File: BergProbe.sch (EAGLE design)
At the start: 16 parts, among them Q1 DMG6602SVT, Q2 DMG6602SVT, U1 DS3231SN

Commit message: Initial (incomplete) PCB Layout.
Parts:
- renumbered R5 to R500, R6 to R600
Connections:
- removed net BATTERY: R500.1, R600.2, U$1.BAT
- net SAT_BAT: now also R500.1, R600.2, U$1.BAT
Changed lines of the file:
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@@
 <part name="GND10" library="supply1" deviceset="GND" device=""/>
 <part name="Q1" library="farnell-parts" deviceset="DMG6602SVT" device=""/>
-<part name="R5" library="resistor" deviceset="R-EU_" device="R0805" value="DNP"/>
-<part name="R6" library="resistor" deviceset="R-EU_" device="R0805" value="DNP"/>
+<part name="R500" library="resistor" deviceset="R-EU_" device="R0805" value="DNP"/>
+<part name="R600" library="resistor" deviceset="R-EU_" device="R0805" value="DNP"/>
 </parts>
 <sheets>
@@
 <instance part="Q1" gate="G$1" x="342.9" y="190.5"/>
 <instance part="Q1" gate="G$2" x="347.98" y="198.12"/>
-<instance part="R5" gate="G$1" x="119.38" y="50.8" rot="R180"/>
-<instance part="R6" gate="G$1" x="134.62" y="50.8" rot="R180"/>
+<instance part="R500" gate="G$1" x="119.38" y="50.8" rot="R180"/>
+<instance part="R600" gate="G$1" x="134.62" y="50.8" rot="R180"/>
 </instances>
 <busses>
 </busses>
 <nets>
-<net name="BATTERY" class="0">
-<segment>
-<pinref part="U$1" gate="G$1" pin="BAT"/>
-<wire x1="38.1" y1="218.44" x2="38.1" y2="246.38" width="0.1524" layer="91"/>
-<label x="38.1" y="233.68" size="1.778" layer="95" rot="R90"/>
-</segment>
-<segment>
-<pinref part="R6" gate="G$1" pin="2"/>
-<pinref part="R5" gate="G$1" pin="1"/>
-<wire x1="129.54" y1="50.8" x2="127" y2="50.8" width="0.1524" layer="91"/>
-<wire x1="127" y1="50.8" x2="124.46" y2="50.8" width="0.1524" layer="91"/>
-<wire x1="127" y1="50.8" x2="127" y2="35.56" width="0.1524" layer="91"/>
-<label x="127" y="35.56" size="1.778" layer="95" rot="R90"/>
-</segment>
-</net>
 <net name="GND" class="0">
 <segment>
@@
 </segment>
 <segment>
-<pinref part="R5" gate="G$1" pin="2"/>
-<wire x1="114.3" y1="50.8" x2="101.6" y2="50.8" width="0.1524" layer="91"/>
+<pinref part="R500" gate="G$1" pin="2"/>
+<wire x1="114.3" y1="50.8" x2="111.76" y2="50.8" width="0.1524" layer="91"/>
 <label x="101.6" y="50.8" size="1.778" layer="95"/>
+<wire x1="111.76" y1="50.8" x2="101.6" y2="50.8" width="0.1524" layer="91"/>
+<wire x1="111.76" y1="50.8" x2="111.76" y2="48.26" width="0.1524" layer="91"/>
+<pinref part="R600" gate="G$1" pin="2"/>
+<pinref part="R500" gate="G$1" pin="1"/>
+<wire x1="129.54" y1="50.8" x2="127" y2="50.8" width="0.1524" layer="91"/>
+<wire x1="127" y1="50.8" x2="124.46" y2="50.8" width="0.1524" layer="91"/>
+<wire x1="127" y1="50.8" x2="127" y2="48.26" width="0.1524" layer="91"/>
+<label x="127" y="35.56" size="1.778" layer="95" rot="R90"/>
+<wire x1="127" y1="48.26" x2="127" y2="35.56" width="0.1524" layer="91"/>
+<wire x1="111.76" y1="48.26" x2="127" y2="48.26" width="0.1524" layer="91"/>
+<junction x="111.76" y="50.8"/>
+<junction x="127" y="48.26"/>
+</segment>
+<segment>
+<pinref part="U$1" gate="G$1" pin="BAT"/>
+<wire x1="38.1" y1="218.44" x2="38.1" y2="246.38" width="0.1524" layer="91"/>
+<label x="38.1" y="233.68" size="1.778" layer="95" rot="R90"/>
 </segment>
 </net>
@@
 </segment>
 <segment>
-<pinref part="R6" gate="G$1" pin="1"/>
+<pinref part="R600" gate="G$1" pin="1"/>
 <wire x1="139.7" y1="50.8" x2="152.4" y2="50.8" width="0.1524" layer="91"/>
 <label x="142.24" y="50.8" size="1.778" layer="95"/>

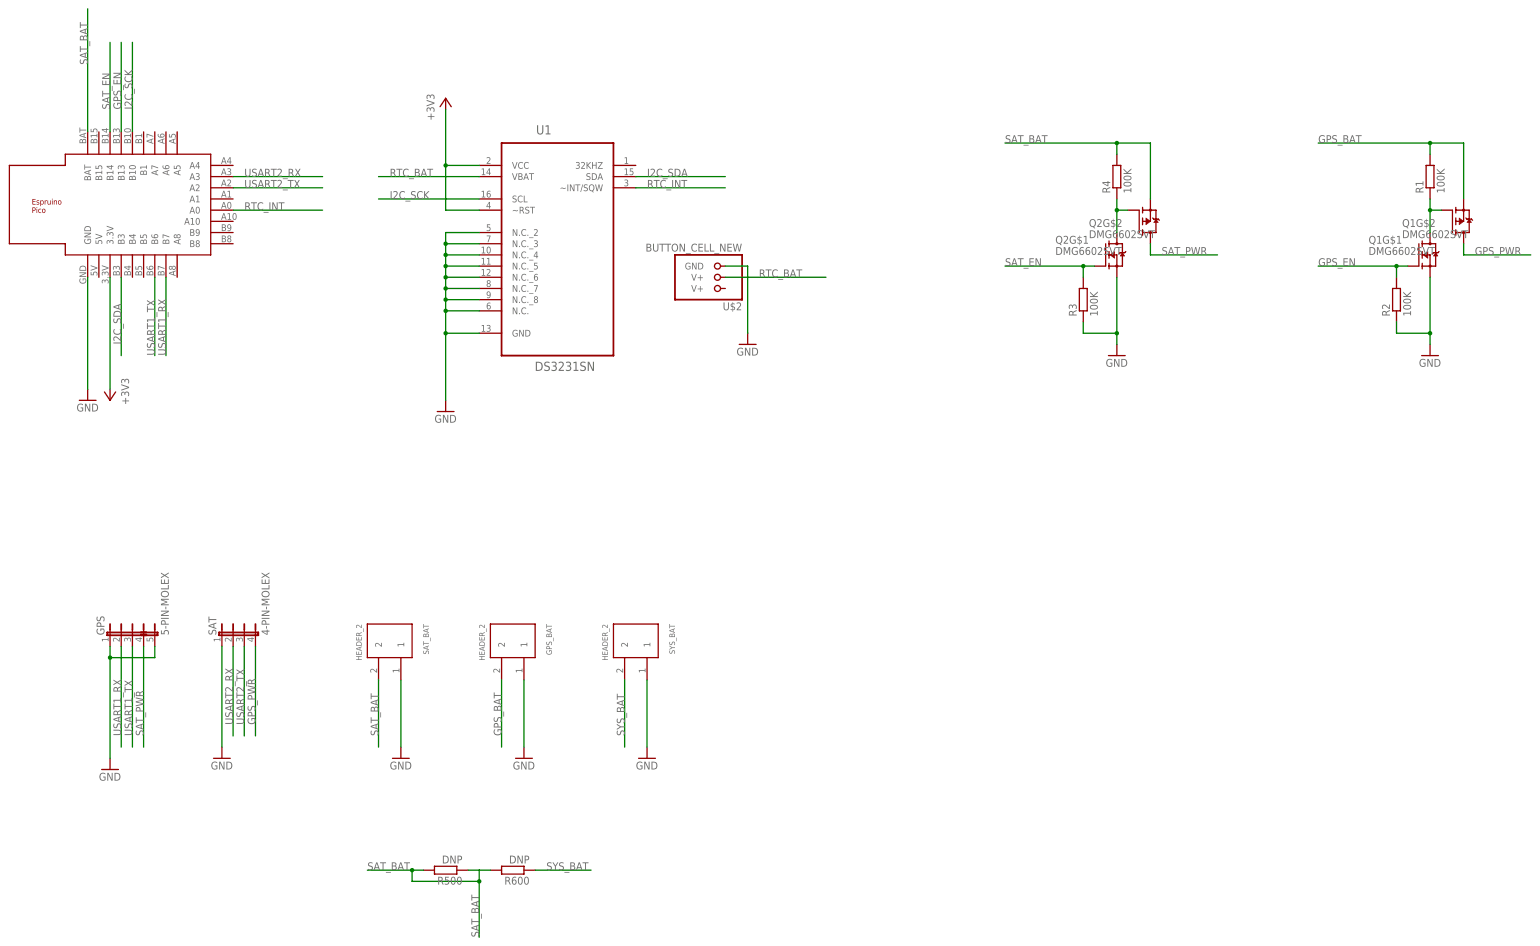
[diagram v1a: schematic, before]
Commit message: Progress on PCB layout. Added analogue headers to schematic.
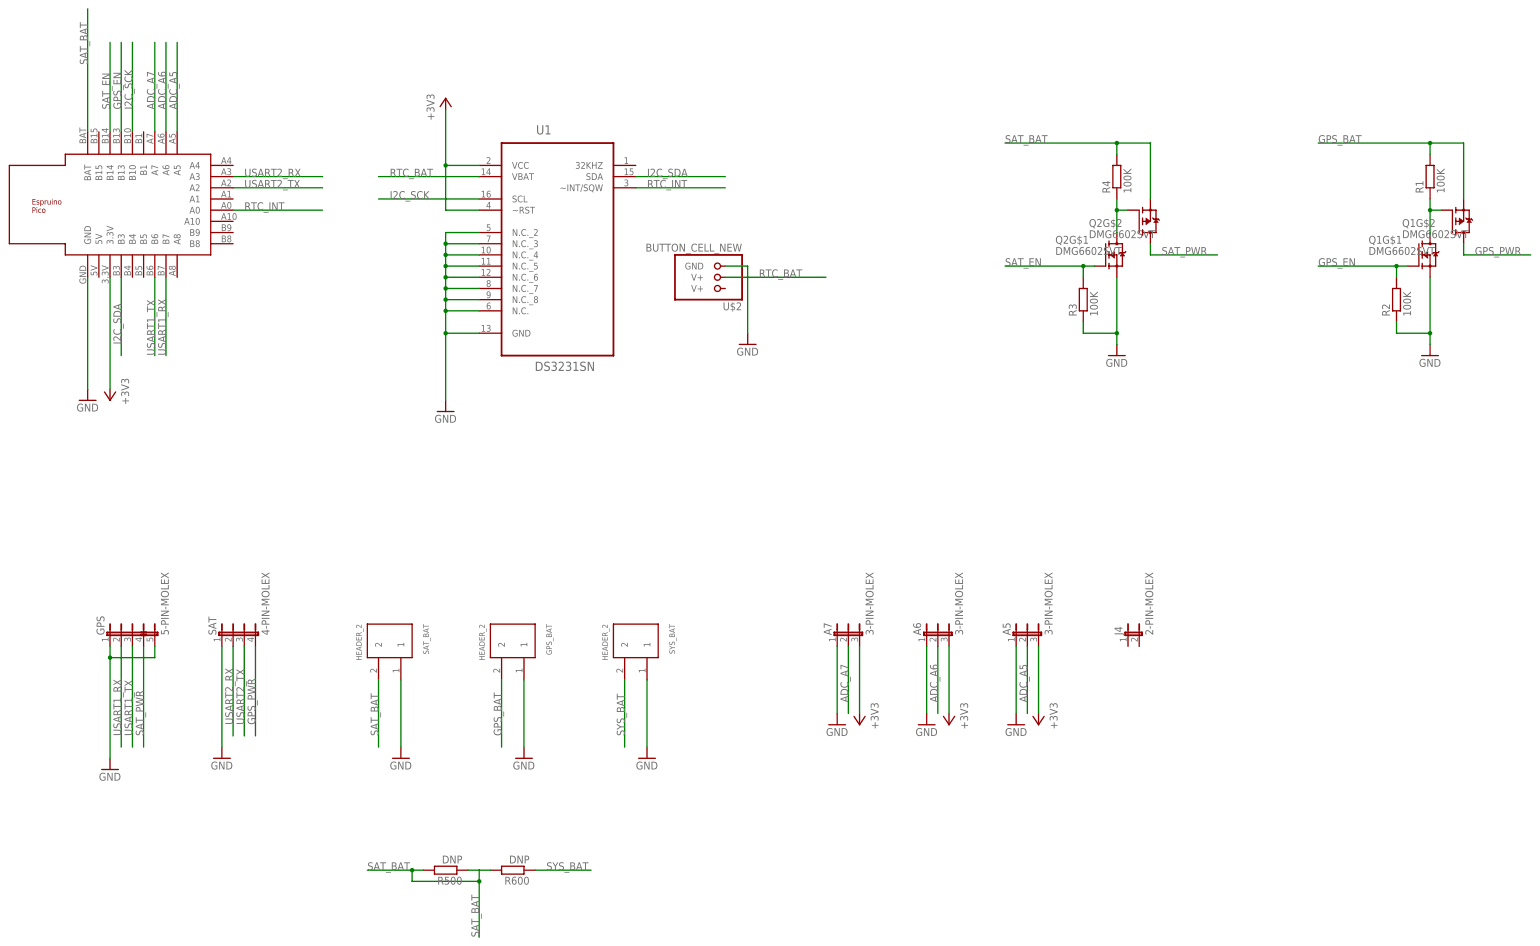
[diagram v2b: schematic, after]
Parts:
- added A5, A6, A7: 3-PIN-MOLEX, farnell-parts:3-PIN-MOLEX
- added J4: 2-PIN-MOLEX, farnell-parts:2-PIN-MOLEX
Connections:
- new net ADC_A5: A5.2, U$1.A5
- new net ADC_A6: A6.2, U$1.A6
- new net ADC_A7: A7.2, U$1.A7
- net +3V3: now also A5.3, A6.3, A7.3
- net GND: now also A5.1, A6.1, A7.1
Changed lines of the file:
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@@
 <part name="R500" library="resistor" deviceset="R-EU_" device="R0805" value="DNP"/>
 <part name="R600" library="resistor" deviceset="R-EU_" device="R0805" value="DNP"/>
+<part name="A7" library="farnell-parts" deviceset="3-PIN-MOLEX" device=""/>
+<part name="A6" library="farnell-parts" deviceset="3-PIN-MOLEX" device=""/>
+<part name="A5" library="farnell-parts" deviceset="3-PIN-MOLEX" device=""/>
+<part name="J4" library="farnell-parts" deviceset="2-PIN-MOLEX" device=""/>
+<part name="GND11" library="supply1" deviceset="GND" device=""/>
+<part name="GND12" library="supply1" deviceset="GND" device=""/>
+<part name="GND13" library="supply1" deviceset="GND" device=""/>
+<part name="+3V3" library="supply1" deviceset="+3V3" device=""/>
+<part name="+3V4" library="supply1" deviceset="+3V3" device=""/>
+<part name="+3V5" library="supply1" deviceset="+3V3" device=""/>
 </parts>
 <sheets>
@@
 <instance part="R500" gate="G$1" x="119.38" y="50.8" rot="R180"/>
 <instance part="R600" gate="G$1" x="134.62" y="50.8" rot="R180"/>
+<instance part="A7" gate="G$1" x="210.82" y="104.14"/>
+<instance part="A6" gate="G$1" x="231.14" y="104.14"/>
+<instance part="A5" gate="G$1" x="251.46" y="104.14"/>
+<instance part="J4" gate="G$1" x="274.32" y="104.14"/>
+<instance part="GND11" gate="1" x="208.28" y="83.82"/>
+<instance part="GND12" gate="1" x="228.6" y="83.82"/>
+<instance part="GND13" gate="1" x="248.92" y="83.82"/>
+<instance part="+3V3" gate="G$1" x="213.36" y="83.82" rot="R180"/>
+<instance part="+3V4" gate="G$1" x="233.68" y="83.82" rot="R180"/>
+<instance part="+3V5" gate="G$1" x="254" y="83.82" rot="R180"/>
 </instances>
 <busses>
@@
 <wire x1="342.9" y1="172.72" x2="335.28" y2="172.72" width="0.1524" layer="91"/>
 </segment>
+<segment>
+<pinref part="A7" gate="G$1" pin="1"/>
+<wire x1="208.28" y1="101.6" x2="208.28" y2="86.36" width="0.1524" layer="91"/>
+<pinref part="GND11" gate="1" pin="GND"/>
+</segment>
+<segment>
+<pinref part="A6" gate="G$1" pin="1"/>
+<wire x1="228.6" y1="101.6" x2="228.6" y2="86.36" width="0.1524" layer="91"/>
+<pinref part="GND12" gate="1" pin="GND"/>
+</segment>
+<segment>
+<pinref part="A5" gate="G$1" pin="1"/>
+<wire x1="248.92" y1="101.6" x2="248.92" y2="86.36" width="0.1524" layer="91"/>
+<pinref part="GND13" gate="1" pin="GND"/>
+</segment>
 </net>
 <net name="+3V3" class="0">
@@
 <wire x1="119.38" y1="210.82" x2="119.38" y2="200.66" width="0.1524" layer="91"/>
 <junction x="119.38" y="210.82"/>
+</segment>
+<segment>
+<pinref part="A7" gate="G$1" pin="3"/>
+<wire x1="213.36" y1="101.6" x2="213.36" y2="86.36" width="0.1524" layer="91"/>
+<pinref part="+3V3" gate="G$1" pin="+3V3"/>
+</segment>
+<segment>
+<pinref part="A6" gate="G$1" pin="3"/>
+<wire x1="233.68" y1="101.6" x2="233.68" y2="86.36" width="0.1524" layer="91"/>
+<pinref part="+3V4" gate="G$1" pin="+3V3"/>
+</segment>
+<segment>
+<pinref part="A5" gate="G$1" pin="3"/>
+<wire x1="254" y1="101.6" x2="254" y2="86.36" width="0.1524" layer="91"/>
+<pinref part="+3V5" gate="G$1" pin="+3V3"/>
 </segment>
 </net>
@@
 </segment>
 </net>
+<net name="ADC_A7" class="0">
+<segment>
+<pinref part="U$1" gate="G$1" pin="A7"/>
+<wire x1="53.34" y1="218.44" x2="53.34" y2="238.76" width="0.1524" layer="91"/>
+<label x="53.34" y="223.52" size="1.778" layer="95" rot="R90"/>
+</segment>
+<segment>
+<pinref part="A7" gate="G$1" pin="2"/>
+<wire x1="210.82" y1="101.6" x2="210.82" y2="86.36" width="0.1524" layer="91"/>
+<label x="210.82" y="88.9" size="1.778" layer="95" rot="R90"/>
+</segment>
+</net>
+<net name="ADC_A6" class="0">
+<segment>
+<pinref part="U$1" gate="G$1" pin="A6"/>
+<wire x1="55.88" y1="218.44" x2="55.88" y2="238.76" width="0.1524" layer="91"/>
+<label x="55.88" y="223.52" size="1.778" layer="95" rot="R90"/>
+</segment>
+<segment>
+<pinref part="A6" gate="G$1" pin="2"/>
+<wire x1="231.14" y1="101.6" x2="231.14" y2="86.36" width="0.1524" layer="91"/>
+<label x="231.14" y="88.9" size="1.778" layer="95" rot="R90"/>
+</segment>
+</net>
+<net name="ADC_A5" class="0">
+<segment>
+<pinref part="U$1" gate="G$1" pin="A5"/>
+<wire x1="58.42" y1="218.44" x2="58.42" y2="238.76" width="0.1524" layer="91"/>
+<label x="58.42" y="223.52" size="1.778" layer="95" rot="R90"/>
+</segment>
+<segment>
+<pinref part="A5" gate="G$1" pin="2"/>
+<wire x1="251.46" y1="101.6" x2="251.46" y2="86.36" width="0.1524" layer="91"/>
+<label x="251.46" y="88.9" size="1.778" layer="95" rot="R90"/>
+</segment>
+</net>

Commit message: PCB Layout complete EXCEPT for wakeup switch/RTC Alarm finalisation.
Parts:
- renumbered J4 to WAKE
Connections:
- new net A1: U$1.A1
- new net A10: U$1.A10
- new net A4: U$1.A4
- new net A8: U$1.A8
- new net B1: U$1.B1
- new net B15: U$1.B15
- new net B4: U$1.B4
- new net B5: U$1.B5
- new net B8: U$1.B8
- new net B9: U$1.B9
- new net N$1: WAKE.1
- new net N$3: WAKE.2
- net GPS_PWR: now also GPS.4; no longer SAT.4
- net SAT_PWR: now also SAT.4; no longer GPS.4
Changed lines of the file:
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@@
 <part name="A6" library="farnell-parts" deviceset="3-PIN-MOLEX" device=""/>
 <part name="A5" library="farnell-parts" deviceset="3-PIN-MOLEX" device=""/>
-<part name="J4" library="farnell-parts" deviceset="2-PIN-MOLEX" device=""/>
+<part name="WAKE" library="farnell-parts" deviceset="2-PIN-MOLEX" device=""/>
 <part name="GND11" library="supply1" deviceset="GND" device=""/>
 <part name="GND12" library="supply1" deviceset="GND" device=""/>
@@
 <instance part="A6" gate="G$1" x="231.14" y="104.14"/>
 <instance part="A5" gate="G$1" x="251.46" y="104.14"/>
-<instance part="J4" gate="G$1" x="274.32" y="104.14"/>
+<instance part="WAKE" gate="G$1" x="274.32" y="104.14"/>
 <instance part="GND11" gate="1" x="208.28" y="83.82"/>
 <instance part="GND12" gate="1" x="228.6" y="83.82"/>
@@
 <net name="SAT_PWR" class="0">
 <segment>
-<pinref part="GPS" gate="G$1" pin="4"/>
-<wire x1="50.8" y1="101.6" x2="50.8" y2="78.74" width="0.1524" layer="91"/>
-<label x="50.8" y="81.28" size="1.778" layer="95" rot="R90"/>
-</segment>
-<segment>
 <pinref part="Q2" gate="G$2" pin="D"/>
 <wire x1="279.4" y1="190.5" x2="279.4" y2="193.04" width="0.1524" layer="91"/>
@@
 <label x="281.94" y="190.5" size="1.778" layer="95"/>
 </segment>
-</net>
-<net name="GPS_PWR" class="0">
 <segment>
 <pinref part="SAT" gate="G$1" pin="4"/>
@@
 <label x="76.2" y="83.82" size="1.778" layer="95" rot="R90"/>
 </segment>
+</net>
+<net name="GPS_PWR" class="0">
 <segment>
 <pinref part="Q1" gate="G$2" pin="D"/>
@@
 <wire x1="350.52" y1="190.5" x2="365.76" y2="190.5" width="0.1524" layer="91"/>
 <label x="353.06" y="190.5" size="1.778" layer="95"/>
+</segment>
+<segment>
+<pinref part="GPS" gate="G$1" pin="4"/>
+<wire x1="50.8" y1="101.6" x2="50.8" y2="78.74" width="0.1524" layer="91"/>
+<label x="50.8" y="81.28" size="1.778" layer="95" rot="R90"/>
 </segment>
 </net>
@@
 </segment>
 </net>
+<net name="N$1" class="0">
+<segment>
+<pinref part="WAKE" gate="G$1" pin="1"/>
+<wire x1="274.32" y1="101.6" x2="274.32" y2="86.36" width="0.1524" layer="91"/>
+</segment>
+</net>
+<net name="N$3" class="0">
+<segment>
+<pinref part="WAKE" gate="G$1" pin="2"/>
+<wire x1="276.86" y1="101.6" x2="276.86" y2="86.36" width="0.1524" layer="91"/>
+</segment>
+</net>
+<net name="A4" class="0">
+<segment>
+<pinref part="U$1" gate="G$1" pin="A4"/>
+<wire x1="71.12" y1="210.82" x2="91.44" y2="210.82" width="0.1524" layer="91"/>
+<label x="73.66" y="210.82" size="1.778" layer="95"/>
+</segment>
+</net>
+<net name="A1" class="0">
+<segment>
+<pinref part="U$1" gate="G$1" pin="A1"/>
+<wire x1="71.12" y1="203.2" x2="91.44" y2="203.2" width="0.1524" layer="91"/>
+<label x="73.66" y="203.2" size="1.778" layer="95"/>
+</segment>
+</net>
+<net name="A10" class="0">
+<segment>
+<pinref part="U$1" gate="G$1" pin="A10"/>
+<wire x1="71.12" y1="198.12" x2="91.44" y2="198.12" width="0.1524" layer="91"/>
+<label x="73.66" y="198.12" size="1.778" layer="95"/>
+</segment>
+</net>
+<net name="B9" class="0">
+<segment>
+<pinref part="U$1" gate="G$1" pin="B9"/>
+<wire x1="71.12" y1="195.58" x2="91.44" y2="195.58" width="0.1524" layer="91"/>
+<label x="73.66" y="195.58" size="1.778" layer="95"/>
+</segment>
+</net>
+<net name="B8" class="0">
+<segment>
+<pinref part="U$1" gate="G$1" pin="B8"/>
+<wire x1="71.12" y1="193.04" x2="91.44" y2="193.04" width="0.1524" layer="91"/>
+<label x="73.66" y="193.04" size="1.778" layer="95"/>
+</segment>
+</net>
+<net name="A8" class="0">
+<segment>
+<pinref part="U$1" gate="G$1" pin="A8"/>
+<wire x1="58.42" y1="185.42" x2="58.42" y2="167.64" width="0.1524" layer="91"/>
+<label x="58.42" y="180.34" size="1.778" layer="95" rot="R90"/>
+</segment>
+</net>
+<net name="B5" class="0">
+<segment>
+<pinref part="U$1" gate="G$1" pin="B5"/>
+<wire x1="50.8" y1="185.42" x2="50.8" y2="167.64" width="0.1524" layer="91"/>
+<label x="50.8" y="180.34" size="1.778" layer="95" rot="R90"/>
+</segment>
+</net>
+<net name="B4" class="0">
+<segment>
+<pinref part="U$1" gate="G$1" pin="B4"/>
+<wire x1="48.26" y1="185.42" x2="48.26" y2="167.64" width="0.1524" layer="91"/>
+<label x="48.26" y="180.34" size="1.778" layer="95" rot="R90"/>
+</segment>
+</net>
+<net name="B15" class="0">
+<segment>
+<pinref part="U$1" gate="G$1" pin="B15"/>
+<wire x1="40.64" y1="218.44" x2="40.64" y2="238.76" width="0.1524" layer="91"/>
+<label x="40.64" y="223.52" size="1.778" layer="95" rot="R90"/>
+</segment>
+</net>
+<net name="B1" class="0">
+<segment>
+<pinref part="U$1" gate="G$1" pin="B1"/>
+<wire x1="50.8" y1="218.44" x2="50.8" y2="238.76" width="0.1524" layer="91"/>
+<label x="50.8" y="223.52" size="1.778" layer="95" rot="R90"/>
+</segment>
+</net>

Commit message: FInal PCB and schematic version
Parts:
- added Q3: DMG6602SVT, farnell-parts:DMG6602SVT
- added R5, R6: 100K, resistor:R-EU_R0805
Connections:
- removed net N$1: WAKE.1
- removed net N$3: WAKE.2
- new net WAKE: Q3G$2.D, R6.2, U$1.A0
- net +3V3: now also Q3G$2.S, R5.2
- net GND: now also Q3G$1.D@1, Q3G$1.G, Q3G$1.S, R6.1, WAKE.1
- net RTC_INT: now also Q3G$2.G, R5.1, WAKE.2; no longer U$1.A0
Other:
- moved on the sheet: A5, A6, A7, Q1G$1, Q1G$2, Q2G$1, Q2G$2, R1, R2, R3, R4, R500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
